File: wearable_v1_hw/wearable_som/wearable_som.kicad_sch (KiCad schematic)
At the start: 21 parts, among them IC1 TPS7A0228PDBVR, P1 USB_C_Plug_USB2.0, Q1 PMOS, SW1 Reset, U1 STM32WB55RGVx, U2 BMI270, U3 MCP73831-2-MC, U4 DLF162500LT-5028A1, U5 2450AT18A100E, Y1 Crystal_GND23

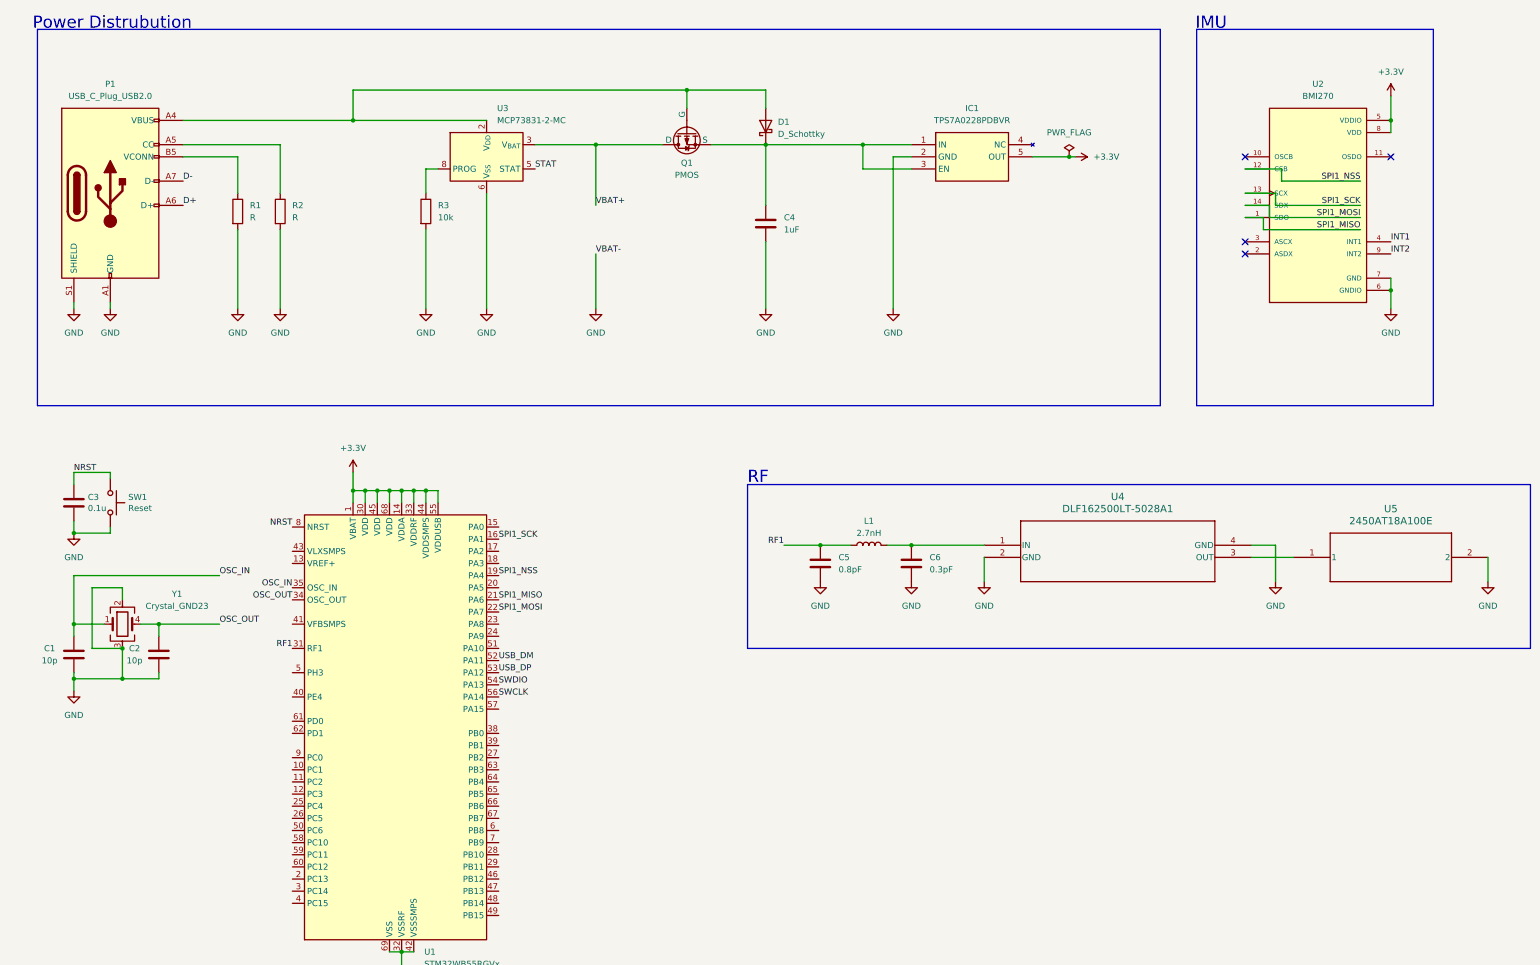
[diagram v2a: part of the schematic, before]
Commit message: 💃added d-,d+ protection, swd, todo statements
💃
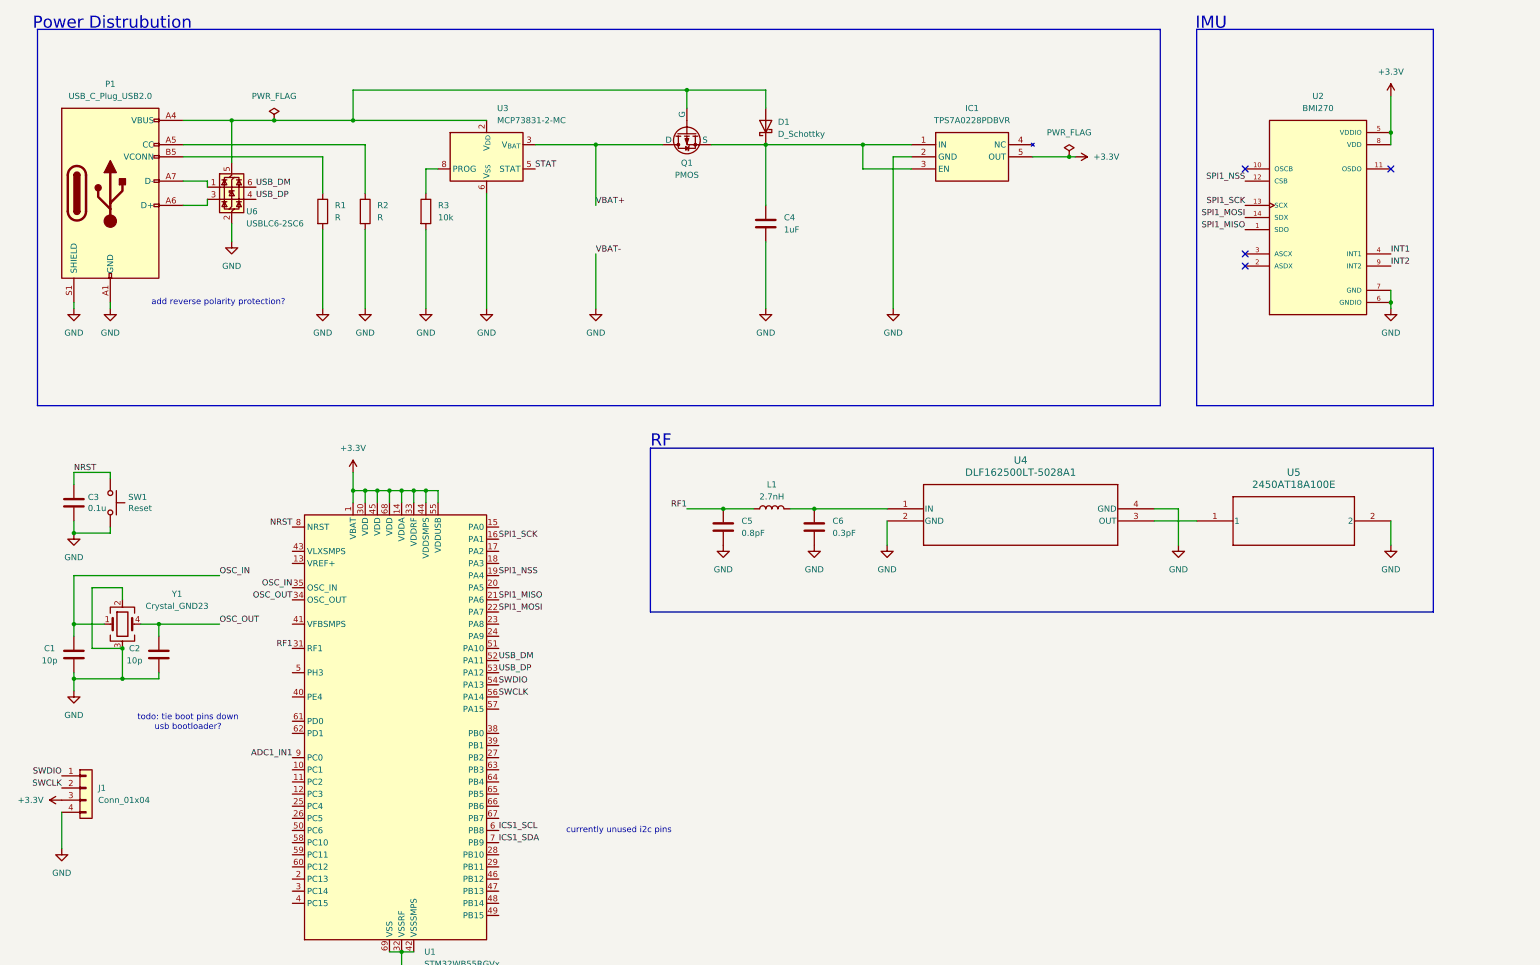
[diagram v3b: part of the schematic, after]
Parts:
- added J1: Conn_01x04, symbol Connector_Generic:Conn_01x04
- added U6: USBLC6-2SC6, Package_TO_SOT_SMD:SOT-23-6, symbol Power_Protection:USBLC6-2SC6
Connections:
- net +3.3V: now also J1.3 (Pin_3)
- net GND: now also J1.4 (Pin_4), U6.2 (GND)
- net SWCLK: now also J1.2 (Pin_2)
- net SWDIO: now also J1.1 (Pin_1)
- net USB_DM: now also U6.6 (I/O1)
- net USB_DP: now also U6.4 (I/O2)
- net at D1.2 (A), P1.A4 (VBUS), P1.A9 (VBUS)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: now also U6.5 (VBUS)
- net ICS1_SCL: now reaches U1.6 (PB8)
- net ICS1_SDA: now reaches U1.7 (PB9)
- net ADC1_IN1: now reaches U1.9 (PC0)
- net D+: no longer names the net of P1.A6 (D+)
- net D+: now also U6.3 (I/O2)
- net D-: no longer names the net of P1.A7 (D-)
- net D-: now also U6.1 (I/O1)
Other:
- note added: "add reverse polarity protection?"
- note added: "currently unused i2c pins"
- note added: "todo: tie boot pins down usb bootloader?"
- moved on the sheet: C5, C6, L1, R1, R2, U2, U4, U5

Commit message: stuff🤓
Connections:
- no-connect marks 4 -> 6
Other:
- note added: "270mV dropout"
- note added: "SOC measurement"
- note added: "not using smps mode"
- note added: "replace with TPS62162 buck"
- moved on the sheet: U1

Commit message: add haptic feedback
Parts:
- added C10, C7, C8, C9: 0.1uF, symbol Device:C
- added D2: LED, symbol Device:LED
- added IC2: DA7280-00FV2, QFN65P300X300X84-12N, symbol wearable-som-sym-lib:DA7280-00FV2
- added M1: Motor_DC, symbol Motor:Motor_DC
- added R4: 4.7k, symbol Device:R
- added R5, R6, R7: 10k, symbol Device:R
- added R8, R9: 4.7, symbol Device:R
- added SW2: SW_Nidec_CAS-120A1, Button_Switch_SMD:Nidec_Copal_CAS-120A, symbol Switch:SW_Nidec_CAS-120A1
- added SW3: Boot, Button_Switch_SMD:SW_SPST_B3SL-1002P, symbol Switch:SW_Push
- R1, R2: value R -> 5.1k
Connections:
- net +3.3V: now also C7.1, C8.1, C9.1, IC2.4 (VDD), IC2.9 (VDDIO), R8.1, R9.1, SW3.2
- net ADC1_IN1: now also R6.2, R7.1
- net GND: now also C10.2, C7.2, C8.2, C9.2, D2.1 (K), IC2.6 (GND_1), IC2.7 (GND_2), R5.2, R7.2, SW2.3 (A)
- net ICS1_SCL: now also IC2.11 (SCL), R8.2
- net ICS1_SDA: now also IC2.10 (SDA), R9.2
- net STAT: now also R6.1
- net VBUS: now reaches D1.2 (A), P1.A4 (VBUS), P1.A9 (VBUS), P1.B4 (VBUS), P1.B9 (VBUS), Q1.2 (G), U3.1 (V_{DD}), U3.2 (V_{DD}), U6.5 (VBUS)
- net VBUS: now also C10.1
- net at C4.1, D1.1 (K), Q1.3 (S): now also SW2.1 (C); no longer IC1.1 (IN), IC1.3 (EN)
- net at U1.5 (PH3): now also R5.1, SW3.1
- net LED0: now reaches U1.51 (PA10)
- net LED0: now also R4.1
- new net: IC1.1 (IN), IC1.3 (EN), SW2.2 (B)
- new net: D2.2 (A), R4.2
- new net: IC2.5 (OUTP), M1.1 (+)
- new net: IC2.8 (OUTN), M1.2 (-)
- new net NIRQ: IC2.12 (NIRQ)
- no-connect marks 6 -> 9
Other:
- note added: "BYPASS CAPS"
- note added: "Haptic feedback"
- note added: "LED output"
- note added: "i2c pull up resistors"
- note removed: "todo: tie boot pins down usb bootloader?"
- moved on the sheet: C1, C2, IC1, Y1

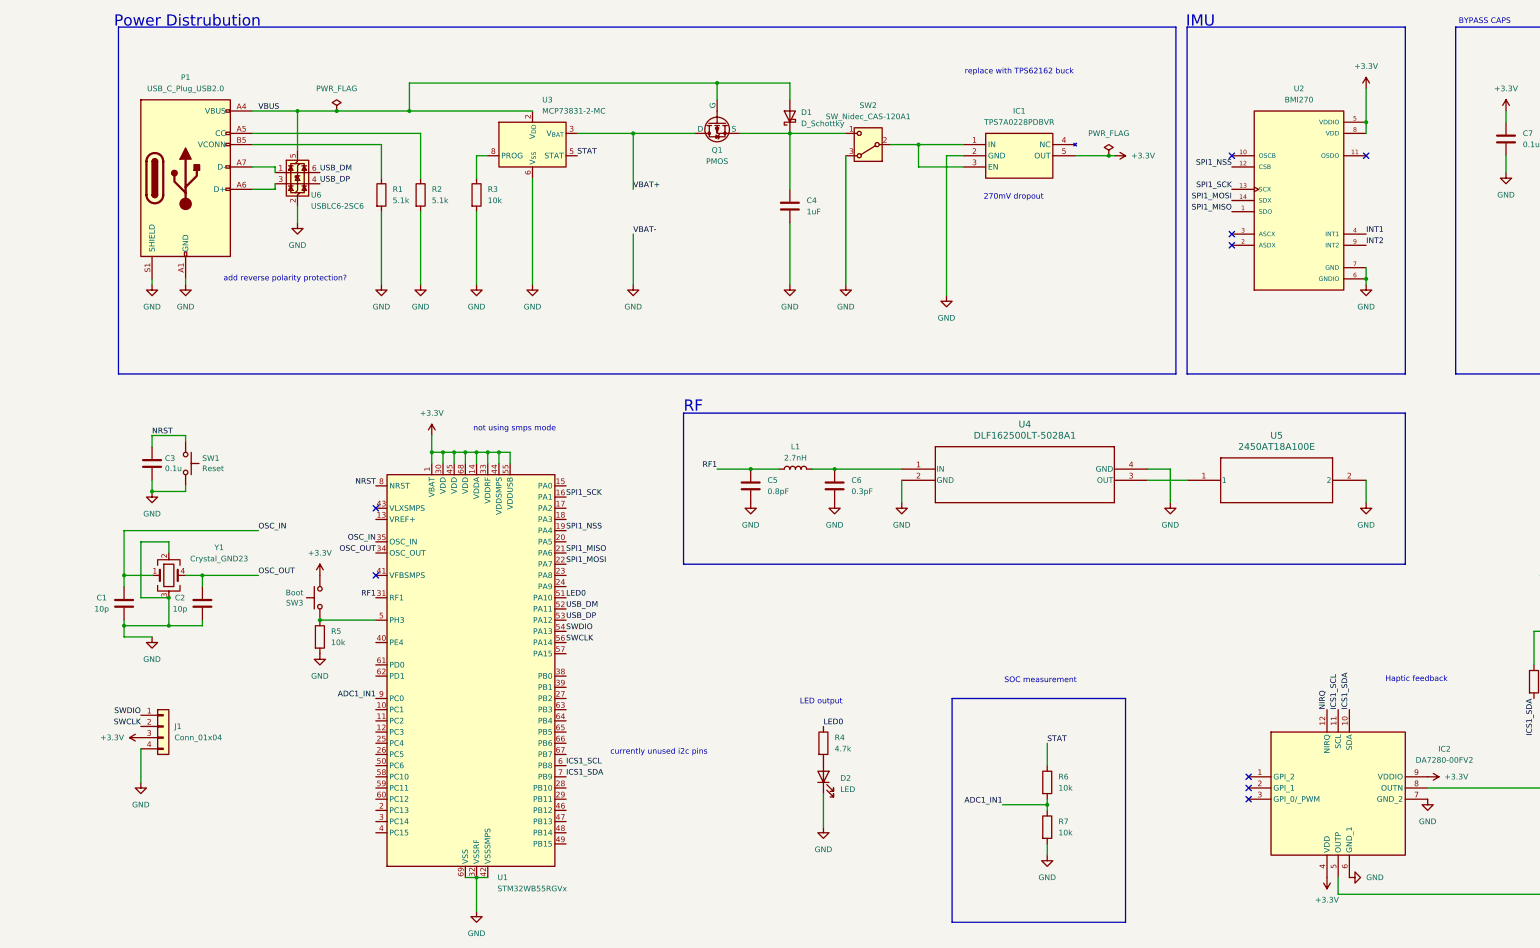
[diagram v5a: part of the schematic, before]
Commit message: pcb layout almost done
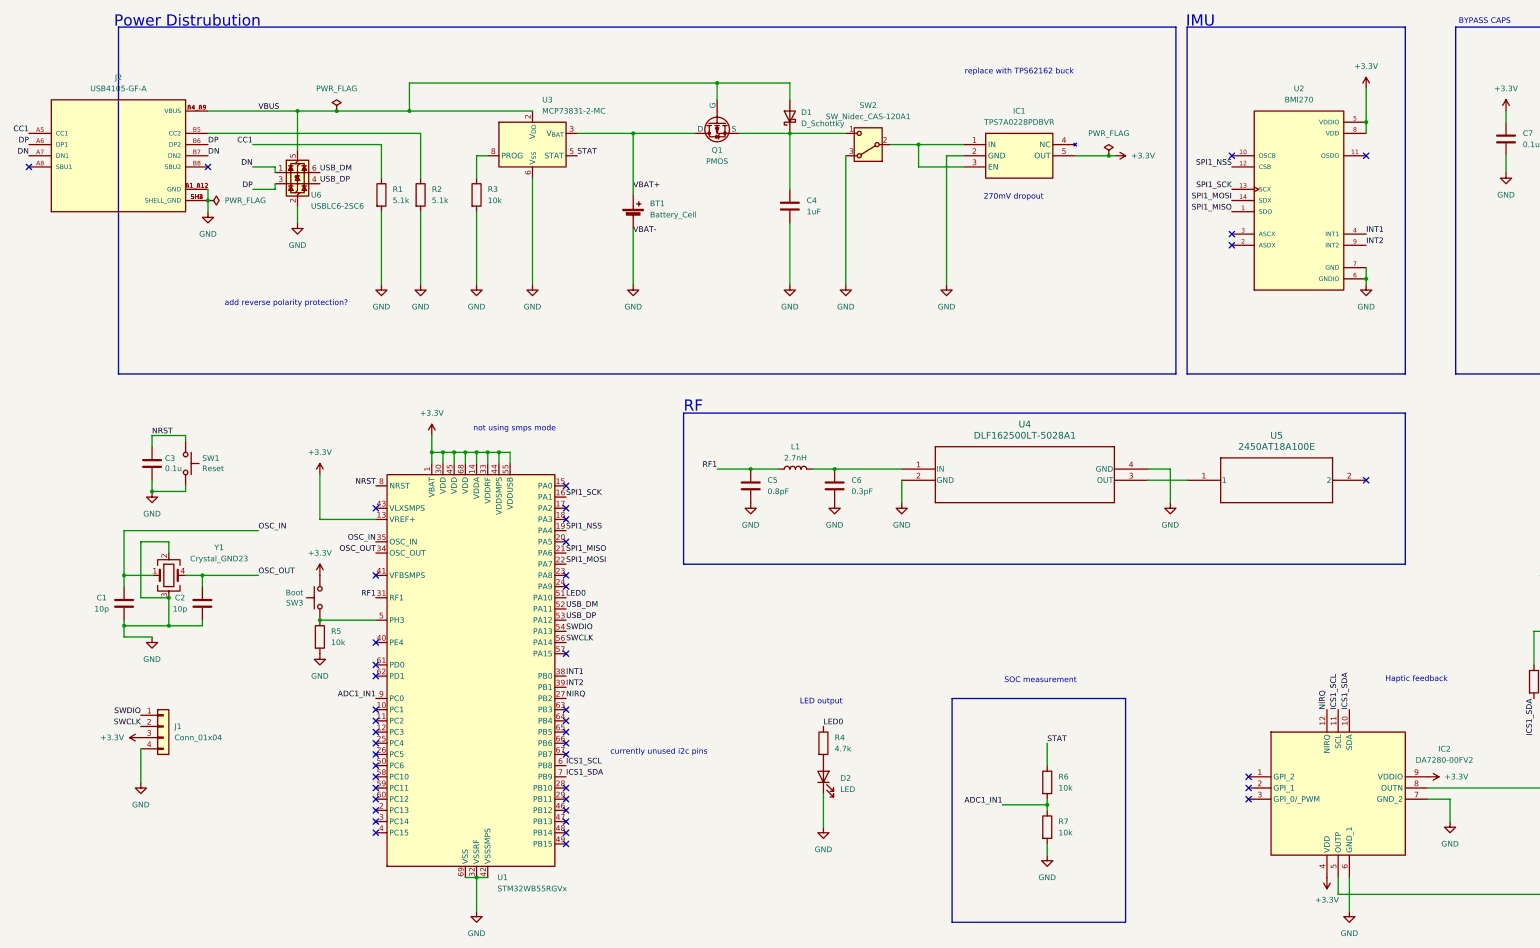
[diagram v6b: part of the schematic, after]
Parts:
- removed P1: USB_C_Plug_USB2.0, symbol Connector:USB_C_Plug_USB2.0
- added BT1: Battery_Cell, Connector_JST:JST_PH_B2B-PH-K_1x02_P2.00mm_Vertical, symbol Device:Battery_Cell
- added J2: USB4105-GF-A, wearable_som_footprint_lib:GCT_USB4105-GF-A, symbol wearable-som-sym-lib:USB4105-GF-A
- C1, C10, C2, C4, C5, C6, C7, C8, C9: footprint (none) -> Capacitor_SMD:C_0805_2012Metric
- D2: footprint (none) -> LED_SMD:LED_0805_2012Metric
- IC2: footprint QFN65P300X300X84-12N -> wearable_som_footprint_lib:QFN65P300X300X84-12N
- J1: footprint (none) -> Connector_PinHeader_2.54mm:PinHeader_1x04_P2.54mm_Vertical
- L1: footprint (none) -> Inductor_SMD:L_0805_2012Metric
- M1: footprint (none) -> TestPoint:TestPoint_2Pads_Pitch5.08mm_Drill1.3mm
- R1, R2, R3, R4, R5, R6, R7, R8, R9: footprint (none) -> Resistor_SMD:R_0805_2012Metric
- U2: footprint BMI270:XDCR_BMI270 -> wearable_som_footprint_lib:XDCR_BMI270
- U4: footprint DLF-4_1P6X0P8 -> wearable_som_footprint_lib:DLF-4_1P6X0P8
- U5: footprint 2450AT18A100E_JOT -> wearable_som_footprint_lib:2450AT18A100E_JOT
- Y1: footprint (none) -> Crystal:Crystal_SMD_0603-4Pin_6.0x3.5mm
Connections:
- net +3.3V: now also U1.13 (VREF+)
- net GND: now also BT1.2 (-), J2.A1_B12 (GND), J2.B1_A12 (GND), J2.SH1 (SHELL_GND), J2.SH2 (SHELL_GND), J2.SH3 (SHELL_GND), J2.SH4 (SHELL_GND); no longer U5.2
- net INT1: now also U1.38 (PB0)
- net INT2: now also U1.39 (PB1)
- net NIRQ: now also U1.27 (PB2)
- net VBAT+: now also BT1.1 (+)
- net VBUS: now also J2.A4_B9 (VBUS), J2.B4_A9 (VBUS)
- net DN: now reaches U6.1 (I/O1)
- net DN: now also J2.A7 (DN1), J2.B7 (DN2)
- net DP: now reaches U6.3 (I/O2)
- net DP: now also J2.A6 (DP1), J2.B6 (DP2)
- net at R2.1: now also J2.B5 (CC2)
- net CC1: now reaches R1.1
- net CC1: now also J2.A5 (CC1)
- no-connect marks 9 -> 45

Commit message: revisions revisions
2->4 layers
improved ground plane + ic placement
added adc for force sensor
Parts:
- removed C9: 0.1uF, Capacitor_SMD:C_0805_2012Metric, symbol Device:C
- added C11: 100nF, Capacitor_SMD:C_0805_2012Metric, symbol Device:C
- added D3: LED, LED_SMD:LED_0805_2012Metric, symbol Device:LED
- added FB1: FerriteBead, Inductor_SMD:L_0805_2012Metric, symbol Device:FerriteBead
- added R10: R_Variable, Connector_PinSocket_2.54mm:PinSocket_1x02_P2.54mm_Horizontal, symbol Device:R_Variable
- added TP1, TP2, TP3: TestPoint, TestPoint:TestPoint_THTPad_1.0x1.0mm_Drill0.5mm, symbol Connector:TestPoint
- added Y2: Crystal, Crystal:Crystal_SMD_MicroCrystal_CC8V-T1A-2Pin_2.0x1.2mm, symbol Device:Crystal
- R6: value 10k -> 4.7k
- Y1: footprint Crystal:Crystal_SMD_0603-4Pin_6.0x3.5mm -> Crystal:Crystal_SMD_2016-4Pin_2.0x1.6mm
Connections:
- net +3.3V: now also FB1.1; no longer U1.14 (VDDA)
- net ADC1_IN1: now also R7.2, R10.1; no longer R6.2, R7.1
- net GND: now also C11.2, D3.1 (K), R10.2; no longer R7.2
- net INT1: now also U1.10 (PC1); no longer U1.38 (PB0)
- net INT2: now also U1.11 (PC2); no longer U1.39 (PB1)
- net OSC_IN: no longer C1.2
- net OSC_OUT: no longer C2.2
- net STAT: now also U1.47 (PB13); no longer R6.1
- net VBAT+: now also TP2.1
- net VBUS: now also TP1.1
- net at C4.1, D1.1 (K), Q1.3 (S)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: now also TP3.1
- net LED1: now reaches U1.23 (PA8)
- net LED1: now also R6.1
- net RCC_OSC32_IN: now reaches U1.3 (PC14)
- net RCC_OSC32_IN: now also C1.2, Y2.1
- net RCC_OSC32_OUT: now reaches U1.4 (PC15)
- net RCC_OSC32_OUT: now also C2.2, Y2.2
- net USB_DM renamed USB_DN
- new net: D3.2 (A), R6.2
- new net +3.3VA: C11.1, FB1.2, R7.1, U1.14 (VDDA)
- no-connect marks 45 -> 41
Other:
- note added: "Foot Force sensing"
- note added: "HSE"
- note added: "VDDA Separation"
- note removed: "SOC measurement"
- moved on the sheet: BT1, C10, C3, C4, C5, C6, C7, C8, D1, D2, IC1, IC2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
